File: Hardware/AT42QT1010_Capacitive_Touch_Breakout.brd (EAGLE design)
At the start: 25.4 x 33 mm, 28 parts, among them Q1 600mA/40V, U1 AT42QT1010 - UDFN

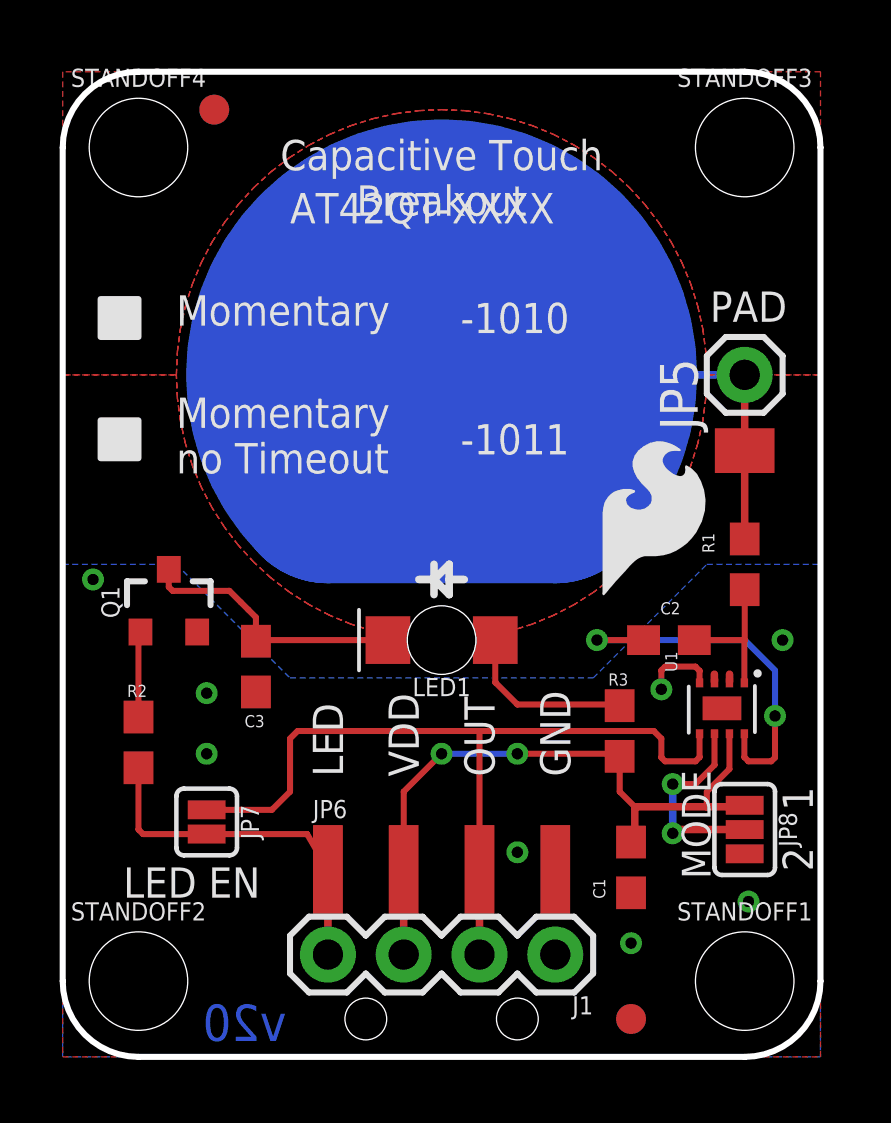
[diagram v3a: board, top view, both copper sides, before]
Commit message: Post Double Check fixes
Moved fiducials again, fixed LED pin routing, deleted strange tRestrict
around LED pin, and adjusted some silk once more.
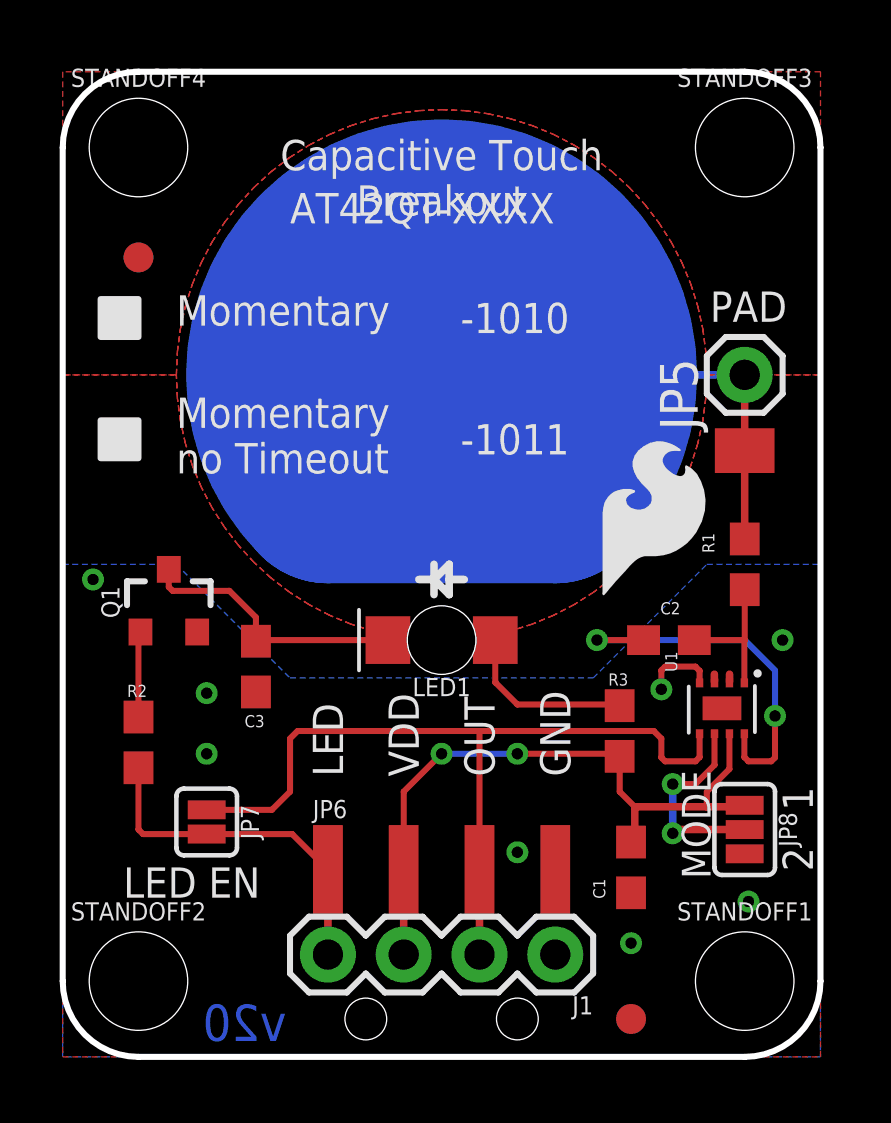
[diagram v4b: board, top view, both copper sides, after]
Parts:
- moved FID1 5.57 mm to (2.54, 26.8)
- moved FID4 5.57 mm to (2.54, 26.8)
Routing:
- net LED: track 13.0 -> 12.4 mm
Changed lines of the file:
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@@
 <text x="16.51" y="5.08" size="1.016" layer="22" font="vector" ratio="15" rot="MR270" align="center-right">GND</text>
 <text x="6.096" y="1.143" size="1.2192" layer="16" font="vector" ratio="15" rot="MR0" align="center">v20</text>
-<text x="22.86" y="24.638" size="1.016" layer="22" font="vector" ratio="15" rot="MR270" align="center-right">PAD</text>
+<text x="21.336" y="25.146" size="1.016" layer="22" font="vector" ratio="15" rot="MR0" align="center-right">PAD</text>
 <text x="12.7" y="28.194" size="1.016" layer="21" font="vector" ratio="19" align="bottom-center">Capacitive Touch
 Breakout
@@
 <rectangle x1="22.098" y1="13.081" x2="22.479" y2="13.589" layer="41"/>
 <rectangle x1="21.971" y1="14.351" x2="22.352" y2="14.859" layer="41"/>
-<rectangle x1="7.62" y1="7.874" x2="8.001" y2="8.382" layer="41"/>
 <text x="3.81" y="24.511" size="1.016" layer="21" font="vector" ratio="15">Momentary</text>
 <text x="3.81" y="19.558" size="1.016" layer="21" font="vector" ratio="15">Momentary
@@
 <attribute name="VALUE" value="Green" x="12.7" y="13.97" size="1.778" layer="27" rot="R180" display="off"/>
 </element>
-<element name="FID1" library="SparkFun-Aesthetics" package="FIDUCIAL-1X2" value="FIDUCIAL1X2" x="5.08" y="31.75"/>
+<element name="FID1" library="SparkFun-Aesthetics" package="FIDUCIAL-1X2" value="FIDUCIAL1X2" x="2.54" y="26.797"/>
 <element name="FID2" library="SparkFun-Aesthetics" package="FIDUCIAL-1X2" value="FIDUCIAL1X2" x="19.05" y="1.27"/>
 <element name="JP9" library="SparkFun-Connectors" package="PAD-1.5X4.5" value="M01SMD-4.5X1.5" x="22.86" y="20.32" smashed="yes" rot="R90"/>
 <element name="JP8" library="SparkFun-Jumpers" package="SMT-JUMPER_3_NO_SILK" value="JUMPER-SMT_3_NO_SILK" x="22.86" y="7.62" rot="R270"/>
 <element name="FID3" library="SparkFun-Aesthetics" package="FIDUCIAL-1X2" value="FIDUCIAL1X2" x="19.05" y="1.27" rot="MR0"/>
-<element name="FID4" library="SparkFun-Aesthetics" package="FIDUCIAL-1X2" value="FIDUCIAL1X2" x="5.08" y="31.75" rot="MR0"/>
+<element name="FID4" library="SparkFun-Aesthetics" package="FIDUCIAL-1X2" value="FIDUCIAL1X2" x="2.54" y="26.797" rot="MR0"/>
 <element name="JP7" library="SparkFun-Jumpers" package="SMT-JUMPER_2_NO_SILK" value="JUMPER-SMT_2_NO_SILK" x="4.826" y="7.874" rot="R270"/>
 <element name="U$1" library="SparkFun-Aesthetics" package="ORDERING_INSTRUCTIONS" value="SPECIAL_INSTRUCTIONS-ORDERING" x="-35.56" y="-21.59"/>
@@
 <wire x1="8.89" y1="3.81" x2="8.89" y2="3.429" width="0.254" layer="16"/>
 <wire x1="8.89" y1="6.27" x2="8.89" y2="3.429" width="0.254" layer="1"/>
-<wire x1="8.6224" y1="6.5024" x2="8.89" y2="6.27" width="0.2032" layer="1"/>
 <wire x1="4.6736" y1="7.62" x2="4.826" y2="7.4676" width="0.2032" layer="1"/>
 <wire x1="4.826" y1="7.4676" x2="2.6924" y2="7.4676" width="0.2032" layer="1"/>
 <wire x1="2.6924" y1="7.4676" x2="2.54" y2="7.62" width="0.2032" layer="1"/>
 <wire x1="2.54" y1="7.62" x2="2.54" y2="9.691" width="0.2032" layer="1"/>
-<wire x1="4.826" y1="7.4676" x2="8.1924" y2="7.4676" width="0.2032" layer="1"/>
-<wire x1="8.1924" y1="7.4676" x2="8.89" y2="6.27" width="0.2032" layer="1"/>
+<wire x1="8.89" y1="6.27" x2="7.6924" y2="7.4676" width="0.2032" layer="1"/>
+<wire x1="7.6924" y1="7.4676" x2="4.826" y2="7.4676" width="0.2032" layer="1"/>
 </signal>
 <signal name="N$4">
@@
 <wire x1="10.9" y1="13.97" x2="6.516" y2="13.97" width="0.2032" layer="1"/>
 <wire x1="6.516" y1="13.97" x2="6.477" y2="13.931" width="0.2032" layer="1"/>
-<wire x1="5.969" y1="15.24" x2="6.223" y2="14.986" width="0.2032" layer="1"/>
-<wire x1="6.223" y1="14.986" x2="6.477" y2="14.732" width="0.2032" layer="1"/>
+<wire x1="5.588" y1="15.621" x2="6.477" y2="14.732" width="0.2032" layer="1"/>
 <wire x1="6.477" y1="14.732" x2="6.477" y2="13.931" width="0.2032" layer="1"/>
 <wire x1="3.556" y1="16.34" x2="3.556" y2="15.748" width="0.2032" layer="1"/>
 <wire x1="3.556" y1="15.748" x2="3.683" y2="15.621" width="0.2032" layer="1"/>
 <wire x1="3.683" y1="15.621" x2="5.588" y2="15.621" width="0.2032" layer="1"/>
-<wire x1="5.588" y1="15.621" x2="5.969" y2="15.24" width="0.2032" layer="1"/>
 </signal>
 <signal name="N$12">

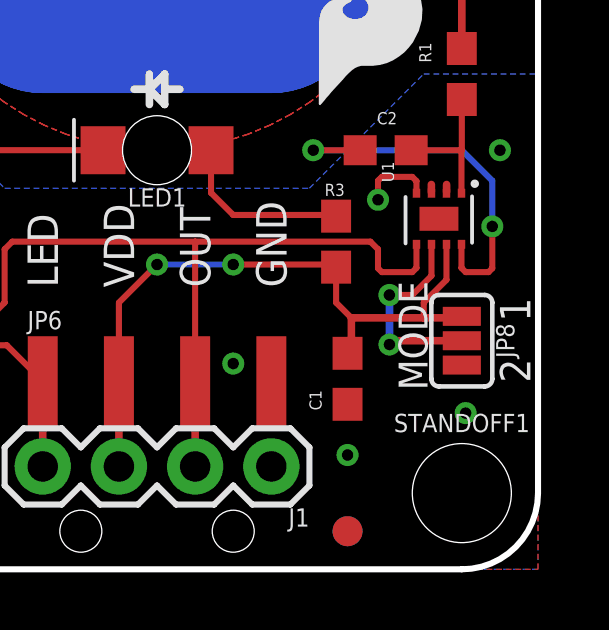
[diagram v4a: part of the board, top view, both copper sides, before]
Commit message: Changed jumpers to be closed jumpers
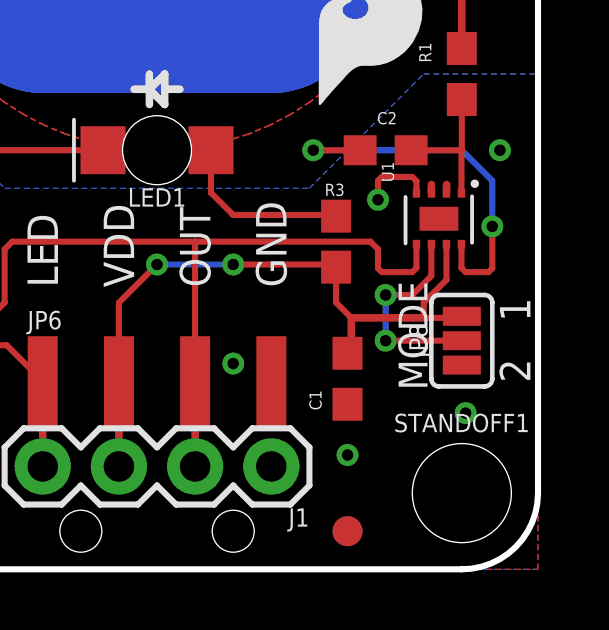
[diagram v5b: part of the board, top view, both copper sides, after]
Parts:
- JP7: value JUMPER-SMT_2_NO_SILK -> JUMPER-SMT_2_NC_PASTE_SILK; device SparkFun-Jumpers:SMT-JUMPER_2_NO_SILK -> SparkFun-Jumpers:SMT-JUMPER_2_NC_PASTE_SILK
- JP8: value JUMPER-SMT_3_NO_SILK -> JUMPER-SMT_3_1-NC_PASTE_SILK; device SparkFun-Jumpers:SMT-JUMPER_3_NO_SILK -> SparkFun-Jumpers:SMT-JUMPER_3_1-NC_PASTE_SILK
- turned JP8 to 90 degrees
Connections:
- net GND: now also JP8.1; no longer JP8.3
- net VCC: now also JP8.3; no longer JP8.1
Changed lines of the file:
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@@
 <layer number="47" name="Measures" color="7" fill="1" visible="no" active="yes"/>
 <layer number="48" name="Document" color="7" fill="1" visible="no" active="yes"/>
-<layer number="49" name="Reference" color="7" fill="1" visible="yes" active="yes"/>
+<layer number="49" name="Reference" color="7" fill="1" visible="no" active="yes"/>
 <layer number="50" name="dxf" color="7" fill="1" visible="no" active="yes"/>
 <layer number="53" name="tGND_GNDA" color="7" fill="9" visible="no" active="no"/>
@@
 <element name="FID2" library="SparkFun-Aesthetics" package="FIDUCIAL-1X2" value="FIDUCIAL1X2" x="19.05" y="1.27"/>
 <element name="JP9" library="SparkFun-Connectors" package="PAD-1.5X4.5" value="M01SMD-4.5X1.5" x="22.86" y="20.32" smashed="yes" rot="R90"/>
-<element name="JP8" library="SparkFun-Jumpers" package="SMT-JUMPER_3_NO_SILK" value="JUMPER-SMT_3_NO_SILK" x="22.86" y="7.62" rot="R270"/>
+<element name="JP8" library="SparkFun-Jumpers" package="SMT-JUMPER_3_1-NC_PASTE_SILK" value="JUMPER-SMT_3_1-NC_PASTE_SILK" x="22.86" y="7.62" rot="R90"/>
 <element name="FID3" library="SparkFun-Aesthetics" package="FIDUCIAL-1X2" value="FIDUCIAL1X2" x="19.05" y="1.27" rot="MR0"/>
 <element name="FID4" library="SparkFun-Aesthetics" package="FIDUCIAL-1X2" value="FIDUCIAL1X2" x="2.54" y="26.797" rot="MR0"/>
-<element name="JP7" library="SparkFun-Jumpers" package="SMT-JUMPER_2_NO_SILK" value="JUMPER-SMT_2_NO_SILK" x="4.826" y="7.874" rot="R270"/>
+<element name="JP7" library="SparkFun-Jumpers" package="SMT-JUMPER_2_NC_PASTE_SILK" value="JUMPER-SMT_2_NC_PASTE_SILK" x="4.826" y="7.874" rot="R270"/>
 <element name="U$1" library="SparkFun-Aesthetics" package="ORDERING_INSTRUCTIONS" value="SPECIAL_INSTRUCTIONS-ORDERING" x="-35.56" y="-21.59"/>
 <element name="J1" library="SparkFun-Connectors" package="1X04" value="" x="16.51" y="3.429" rot="R180">
@@
 <contactref element="U1" pad="7"/>
 <contactref element="JP6" pad="2"/>
-<contactref element="JP8" pad="1"/>
-<wire x1="22.8228" y1="8.47" x2="22.86" y2="8.4328" width="0.254" layer="1"/>
 <wire x1="19.177" y1="8.382" x2="19.177" y2="7.327" width="0.254" layer="1"/>
 <wire x1="19.177" y1="7.327" x2="19.05" y2="7.2" width="0.254" layer="1"/>
 <wire x1="19.177" y1="8.382" x2="21.59" y2="8.382" width="0.254" layer="1"/>
-<wire x1="21.59" y1="8.382" x2="22.8092" y2="8.382" width="0.254" layer="1"/>
-<wire x1="22.8092" y1="8.382" x2="22.86" y2="8.4328" width="0.254" layer="1"/>
 <contactref element="J1" pad="3"/>
 <wire x1="11.43" y1="3.429" x2="11.43" y2="6.27" width="0.254" layer="1"/>
@@
 <wire x1="22.348" y1="9.648" x2="21.59" y2="8.89" width="0.2032" layer="1"/>
 <wire x1="19.177" y1="8.382" x2="18.669" y2="8.89" width="0.2032" layer="1"/>
+<contactref element="JP8" pad="3"/>
+<wire x1="21.59" y1="8.382" x2="22.86" y2="8.382" width="0.2032" layer="1"/>
+<wire x1="22.86" y1="8.382" x2="22.86" y2="8.4328" width="0.2032" layer="1"/>
 </signal>
 <signal name="GND">
@@
 <contactref element="JP6" pad="4"/>
 <via x="19.05" y="3.81" extent="1-16" drill="0.381"/>
-<contactref element="JP8" pad="3"/>
 <via x="1.016" y="16.002" extent="1-16" drill="0.381"/>
 <via x="24.13" y="13.97" extent="1-16" drill="0.381"/>
@@
 <wire x1="20.193" y1="13.081" x2="21.209" y2="13.081" width="0.2032" layer="1"/>
 <via x="15.24" y="6.858" extent="1-16" drill="0.381"/>
+<contactref element="JP8" pad="1"/>
 </signal>
 <signal name="OUT">
@@
 <wire x1="12.954" y1="22.86" x2="22.86" y2="22.86" width="0.254" layer="16"/>
 </signal>
-<signal name="N$7">
-<contactref element="U1" pad="6"/>
-<contactref element="JP8" pad="2"/>
-<wire x1="22.86" y1="7.62" x2="20.574" y2="7.62" width="0.254" layer="1"/>
-<via x="20.447" y="7.493" extent="1-16" drill="0.381"/>
-<wire x1="20.447" y1="7.493" x2="20.447" y2="9.144" width="0.254" layer="16"/>
-<via x="20.447" y="9.144" extent="1-16" drill="0.381"/>
-<wire x1="20.574" y1="7.62" x2="20.447" y2="7.493" width="0.254" layer="1"/>
-<wire x1="21.848" y1="9.783" x2="21.209" y2="9.144" width="0.2032" layer="1"/>
-<wire x1="21.209" y1="9.144" x2="20.447" y2="9.144" width="0.2032" layer="1"/>
-<wire x1="21.848" y1="10.8324" x2="21.848" y2="9.783" width="0.2032" layer="1"/>
-</signal>
 <signal name="N$10">
 <contactref element="R2" pad="2"/>
@@
 <wire x1="22.352" y1="12.573" x2="22.352" y2="12.827" width="0.254" layer="1"/>
 </signal>
+<signal name="N$3">
+<contactref element="U1" pad="6"/>
+<contactref element="JP8" pad="2"/>
+<wire x1="21.848" y1="10.8324" x2="21.844" y2="10.8324" width="0.2032" layer="1"/>
+<wire x1="21.844" y1="10.8324" x2="21.844" y2="9.779" width="0.2032" layer="1"/>
+<wire x1="22.86" y1="7.62" x2="20.32" y2="7.62" width="0.2032" layer="1"/>
+<via x="20.32" y="7.62" extent="1-16" drill="0.381"/>
+<wire x1="20.32" y1="7.62" x2="20.32" y2="9.144" width="0.2032" layer="16"/>
+<wire x1="21.209" y1="9.144" x2="20.32" y2="9.144" width="0.2032" layer="1"/>
+<via x="20.32" y="9.144" extent="1-16" drill="0.381"/>
+<wire x1="21.844" y1="9.779" x2="21.209" y2="9.144" width="0.2032" layer="1"/>
+</signal>
 </signals>
